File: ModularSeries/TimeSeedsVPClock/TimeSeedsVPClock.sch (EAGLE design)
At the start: 75 parts, among them T1 2N3904

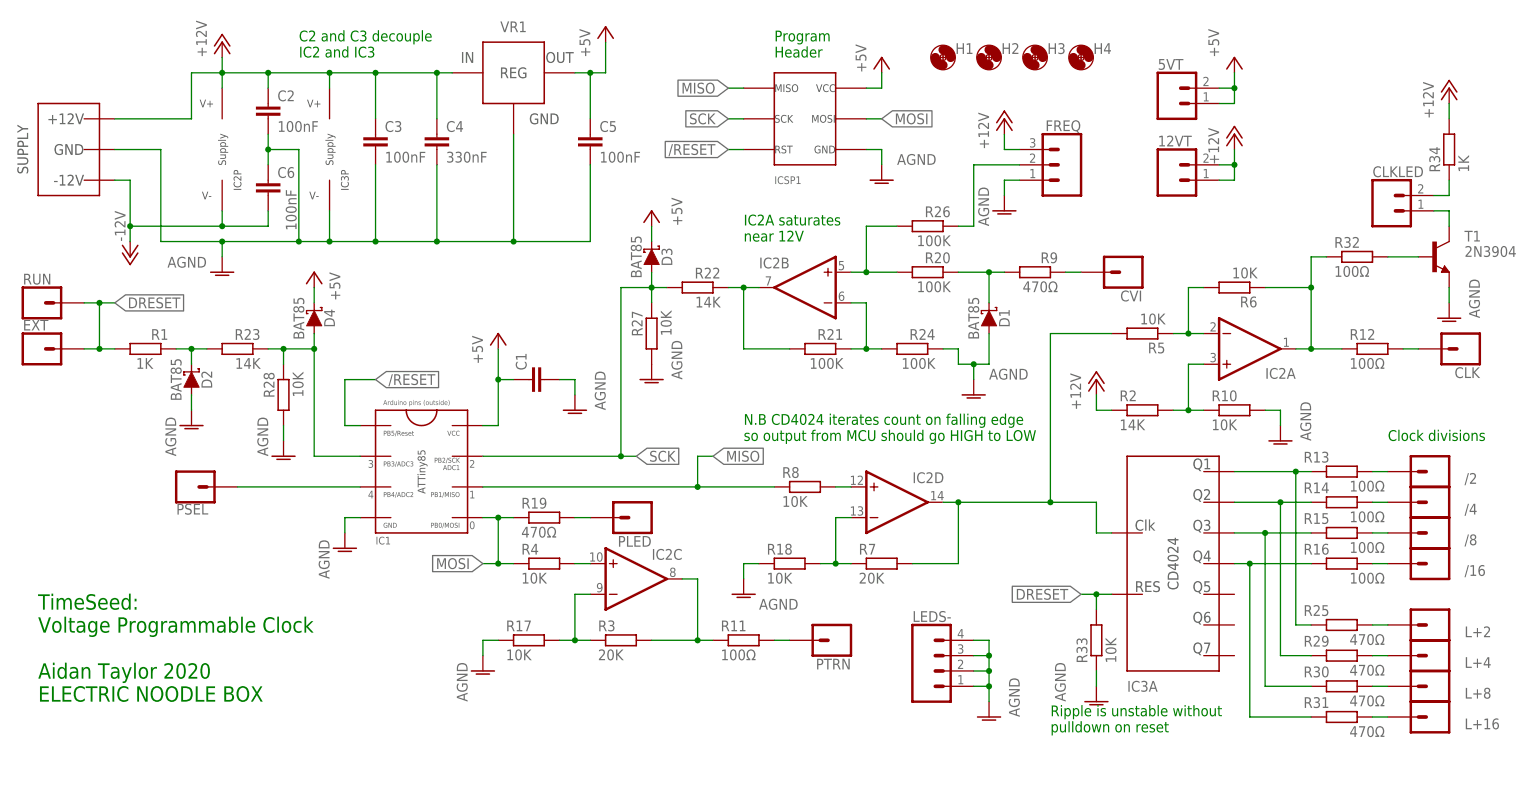
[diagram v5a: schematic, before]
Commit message: Pulse output fixed on Knives, schematics and layout updated. Panel added for Portals
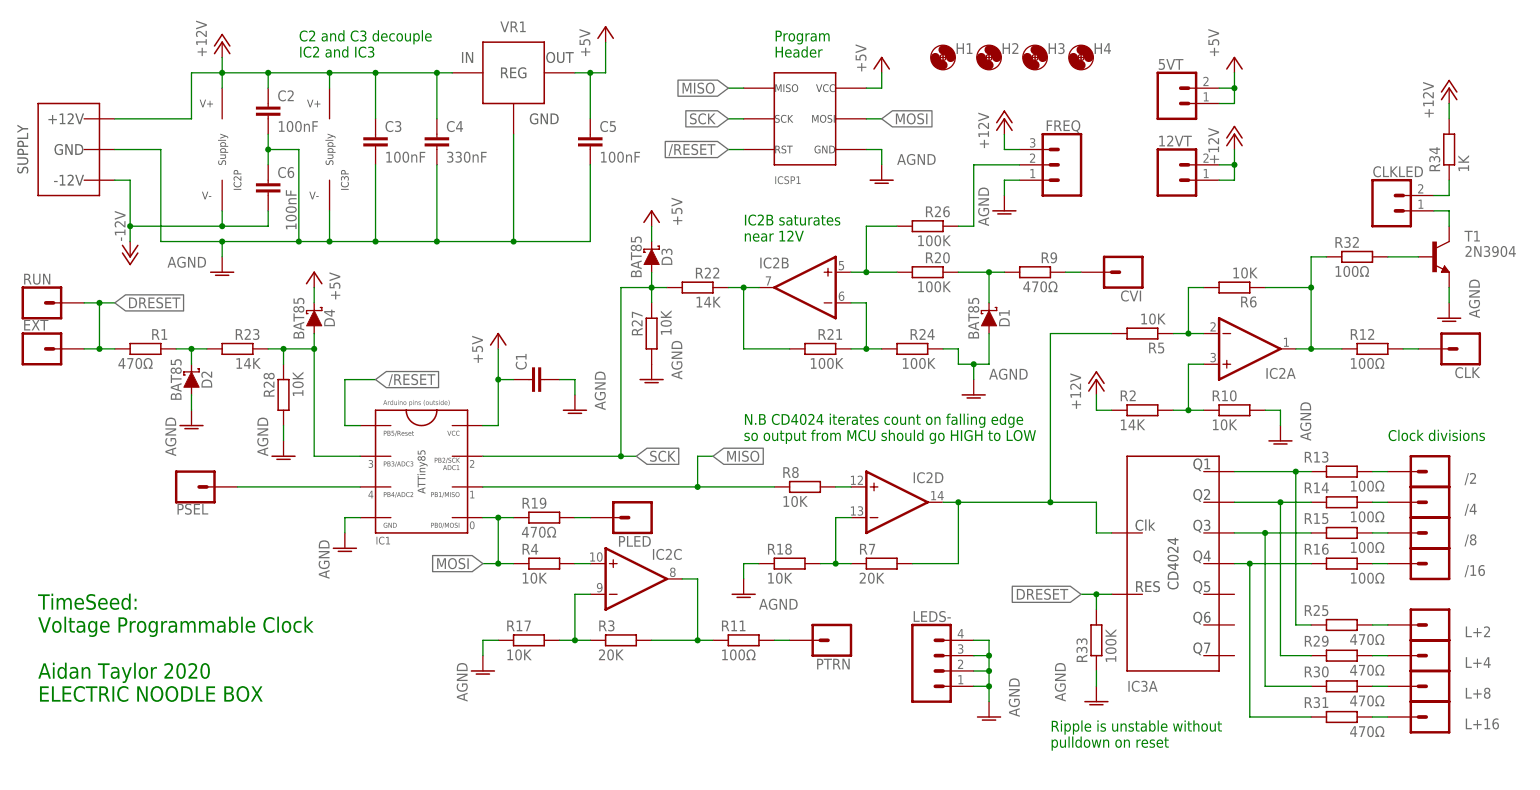
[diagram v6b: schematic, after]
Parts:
- R1: value 1K -> 470Ω
- R33: value 10K -> 100K
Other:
- note added: "IC2B saturates near 12V"
- note removed: "IC2A saturates near 12V"
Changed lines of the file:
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@@
 <part name="D3" library="ElectricNoodleBox" deviceset="SCHOTTKY_DO35" device="" package3d_urn="urn:adsk.eagle:package:43339/2" value="BAT85"/>
 <part name="P+8" library="supply1" library_urn="urn:adsk.eagle:library:371" deviceset="+5V" device=""/>
-<part name="R1" library="rcl" library_urn="urn:adsk.eagle:library:334" deviceset="R-EU_" device="0207/10" package3d_urn="urn:adsk.eagle:package:23491/2" value="1K"/>
+<part name="R1" library="rcl" library_urn="urn:adsk.eagle:library:334" deviceset="R-EU_" device="0207/10" package3d_urn="urn:adsk.eagle:package:23491/2" value="470Ω"/>
 <part name="AGND10" library="supply1" library_urn="urn:adsk.eagle:library:371" deviceset="AGND" device=""/>
 <part name="D4" library="ElectricNoodleBox" deviceset="SCHOTTKY_DO35" device="" package3d_urn="urn:adsk.eagle:package:43339/2" value="BAT85"/>
@@
 <part name="LEDS-" library="ElectricNoodleBox" deviceset="4XWIREPAD" device=""/>
 <part name="AGND7" library="supply1" library_urn="urn:adsk.eagle:library:371" deviceset="AGND" device=""/>
-<part name="R33" library="rcl" library_urn="urn:adsk.eagle:library:334" deviceset="R-EU_" device="0207/10" package3d_urn="urn:adsk.eagle:package:23491/2" value="10K"/>
+<part name="R33" library="rcl" library_urn="urn:adsk.eagle:library:334" deviceset="R-EU_" device="0207/10" package3d_urn="urn:adsk.eagle:package:23491/2" value="100K"/>
 <part name="AGND13" library="supply1" library_urn="urn:adsk.eagle:library:371" deviceset="AGND" device=""/>
 <part name="L+2" library="ElectricNoodleBox" deviceset="1XWIREPAD" device=""/>
@@
 Aidan Taylor 2020
 ELECTRIC NOODLE BOX</text>
-<text x="83.82" y="73.66" size="1.778" layer="91">IC2A saturates
+<text x="83.82" y="73.66" size="1.778" layer="91">IC2B saturates
 near 12V</text>
-<text x="134.62" y="-7.62" size="1.778" layer="91">Ripple is unstable without
+<text x="134.62" y="-10.16" size="1.778" layer="91">Ripple is unstable without
 pulldown on reset</text>
 <text x="83.82" y="40.64" size="1.778" layer="91">N.B CD4024 iterates count on falling edge

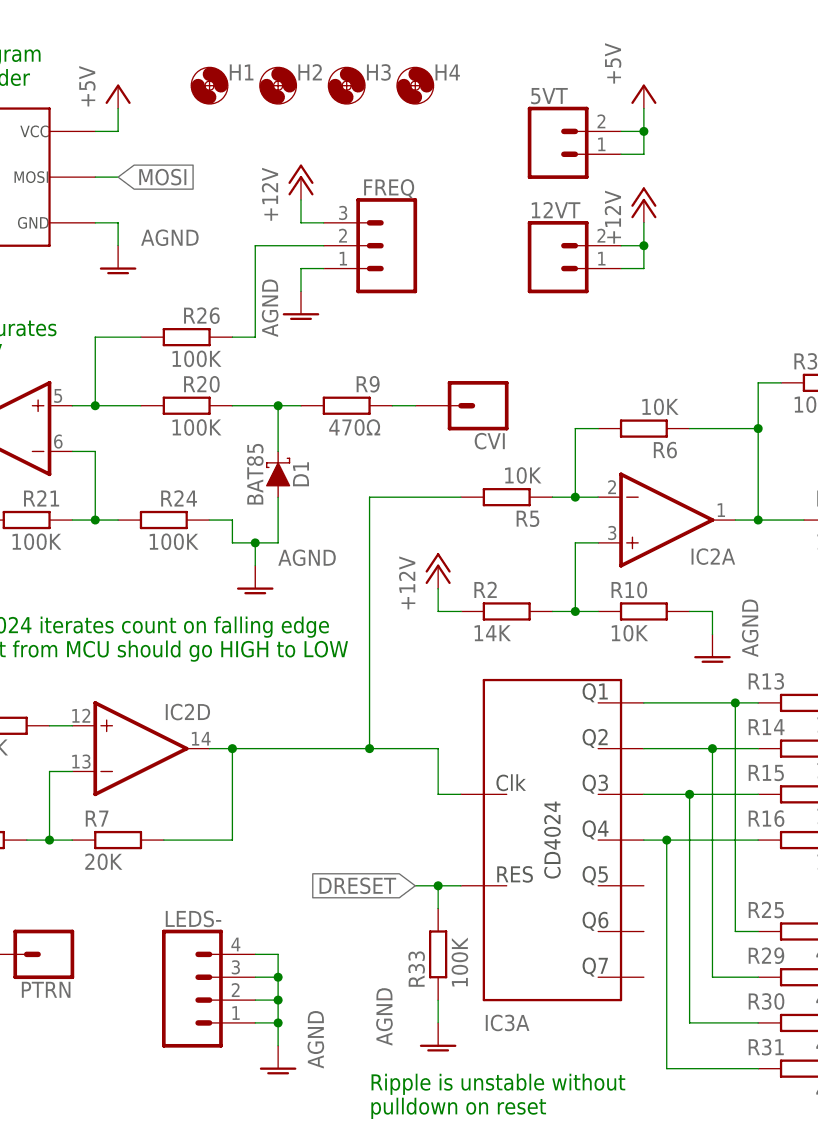
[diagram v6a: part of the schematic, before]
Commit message: Common collector + emitter follower pulse output added to Knives, docs updated
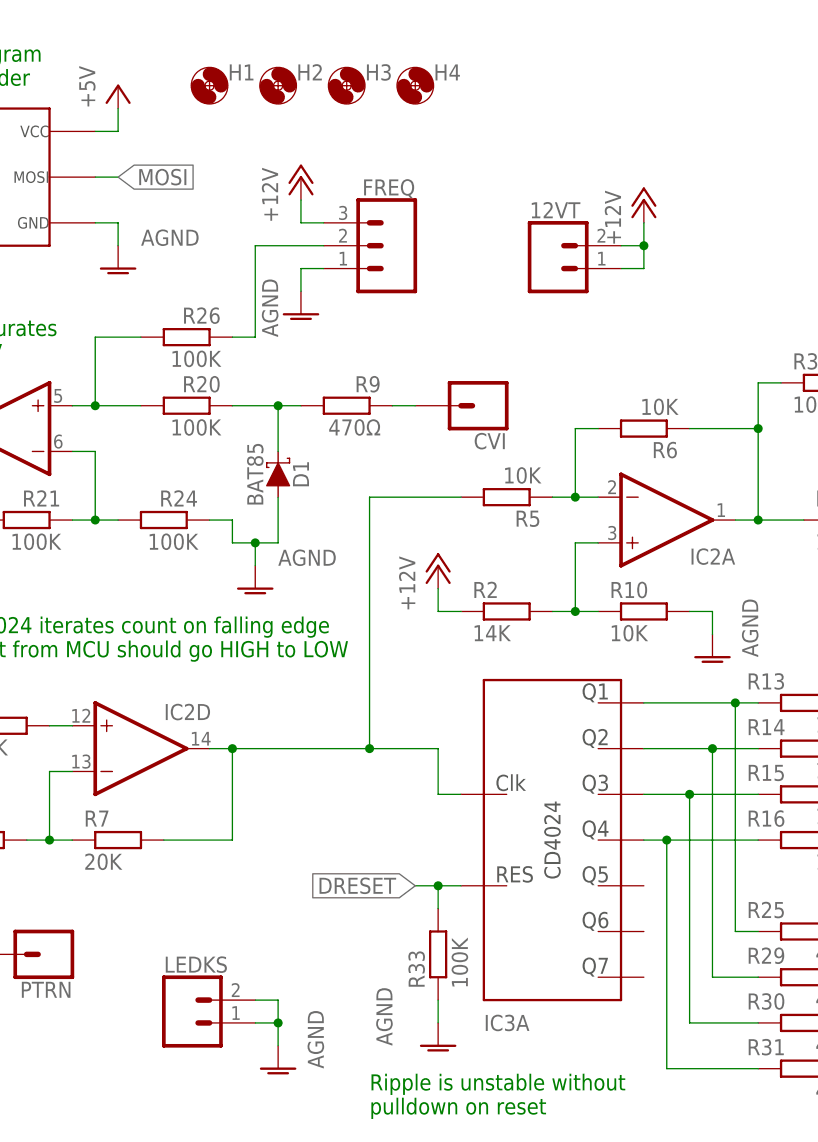
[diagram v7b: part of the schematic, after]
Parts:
- removed 5VT: 2XWIREPAD, ElectricNoodleBox:2XWIREPAD
- removed LEDS-: 4XWIREPAD, ElectricNoodleBox:4XWIREPAD
- added LEDKS: 2XWIREPAD, ElectricNoodleBox:2XWIREPAD
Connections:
- net +5V: no longer 5VT.1, 5VT.2
- net AGND: now also LEDKS.1, LEDKS.2; no longer LEDS-.1, LEDS-.2, LEDS-.3, LEDS-.4
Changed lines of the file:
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@@
 <part name="R31" library="rcl" library_urn="urn:adsk.eagle:library:334" deviceset="R-EU_" device="0207/10" package3d_urn="urn:adsk.eagle:package:23491/2" value="470Ω"/>
 <part name="C6" library="rcl" library_urn="urn:adsk.eagle:library:334" deviceset="C-EU" device="050-025X075" package3d_urn="urn:adsk.eagle:package:23637/1" value="100nF"/>
-<part name="LEDS-" library="ElectricNoodleBox" deviceset="4XWIREPAD" device=""/>
 <part name="AGND7" library="supply1" library_urn="urn:adsk.eagle:library:371" deviceset="AGND" device=""/>
 <part name="R33" library="rcl" library_urn="urn:adsk.eagle:library:334" deviceset="R-EU_" device="0207/10" package3d_urn="urn:adsk.eagle:package:23491/2" value="100K"/>
@@
 <part name="R34" library="rcl" library_urn="urn:adsk.eagle:library:334" deviceset="R-EU_" device="0207/10" package3d_urn="urn:adsk.eagle:package:23491/2" value="1K"/>
 <part name="AGND15" library="supply1" library_urn="urn:adsk.eagle:library:371" deviceset="AGND" device=""/>
-<part name="P+5" library="supply1" library_urn="urn:adsk.eagle:library:371" deviceset="+5V" device=""/>
 <part name="P+11" library="supply1" library_urn="urn:adsk.eagle:library:371" deviceset="+12V" device=""/>
-<part name="5VT" library="ElectricNoodleBox" deviceset="2XWIREPAD" device=""/>
 <part name="12VT" library="ElectricNoodleBox" deviceset="2XWIREPAD" device=""/>
 <part name="WP1" library="ElectricNoodleBox" deviceset="COMBO_SUPPLY_HEADER" device=""/>
+<part name="LEDKS" library="ElectricNoodleBox" deviceset="2XWIREPAD" device=""/>
 </parts>
 <sheets>
@@
 <attribute name="VALUE" x="8.001" y="82.296" size="1.778" layer="96" rot="R270"/>
 </instance>
-<instance part="LEDS-" gate="G$1" x="116.84" y="2.54" smashed="yes">
-<attribute name="NAME" x="111.76" y="10.668" size="1.778" layer="95" font="vector"/>
-</instance>
 <instance part="AGND7" gate="VR1" x="124.46" y="-5.08" smashed="yes">
 <attribute name="VALUE" x="129.54" y="-5.08" size="1.778" layer="96" rot="R90"/>
@@
 <attribute name="VALUE" x="-5.08" y="71.12" size="1.778" layer="96" rot="R180"/>
 </instance>
-<instance part="P+5" gate="1" x="165.1" y="104.14" smashed="yes">
-<attribute name="VALUE" x="162.56" y="104.14" size="1.778" layer="96" rot="R90"/>
-</instance>
 <instance part="P+11" gate="1" x="165.1" y="91.44" smashed="yes">
 <attribute name="VALUE" x="162.56" y="86.36" size="1.778" layer="96" rot="R90"/>
 </instance>
-<instance part="5VT" gate="G$1" x="154.94" y="96.52" smashed="yes">
-<attribute name="NAME" x="152.4" y="102.108" size="1.778" layer="95" font="vector"/>
-</instance>
 <instance part="12VT" gate="G$1" x="154.94" y="83.82" smashed="yes">
 <attribute name="NAME" x="152.4" y="89.408" size="1.778" layer="95" font="vector"/>
 </instance>
 <instance part="WP1" gate="G$1" x="-27.94" y="88.9" smashed="yes" rot="MR0"/>
+<instance part="LEDKS" gate="G$1" x="114.3" y="0" smashed="yes">
+<attribute name="NAME" x="111.76" y="5.588" size="1.778" layer="95" font="vector"/>
+</instance>
 </instances>
 <busses>
@@
 </segment>
 <segment>
-<pinref part="LEDS-" gate="G$1" pin="4"/>
-<wire x1="121.92" y1="7.62" x2="124.46" y2="7.62" width="0.1524" layer="91"/>
-<wire x1="124.46" y1="7.62" x2="124.46" y2="5.08" width="0.1524" layer="91"/>
-<pinref part="LEDS-" gate="G$1" pin="1"/>
-<wire x1="124.46" y1="5.08" x2="124.46" y2="2.54" width="0.1524" layer="91"/>
 <wire x1="124.46" y1="2.54" x2="124.46" y2="0" width="0.1524" layer="91"/>
 <wire x1="124.46" y1="0" x2="121.92" y2="0" width="0.1524" layer="91"/>
-<pinref part="LEDS-" gate="G$1" pin="2"/>
 <wire x1="121.92" y1="2.54" x2="124.46" y2="2.54" width="0.1524" layer="91"/>
-<junction x="124.46" y="2.54"/>
-<pinref part="LEDS-" gate="G$1" pin="3"/>
-<wire x1="121.92" y1="5.08" x2="124.46" y2="5.08" width="0.1524" layer="91"/>
-<junction x="124.46" y="5.08"/>
 <pinref part="AGND7" gate="VR1" pin="AGND"/>
 <wire x1="124.46" y1="0" x2="124.46" y2="-2.54" width="0.1524" layer="91"/>
 <junction x="124.46" y="0"/>
+<pinref part="LEDKS" gate="G$1" pin="1"/>
+<pinref part="LEDKS" gate="G$1" pin="2"/>
 </segment>
 <segment>
@@
 <wire x1="12.7" y1="66.04" x2="12.7" y2="63.5" width="0.1524" layer="91"/>
 </segment>
-<segment>
-<pinref part="5VT" gate="G$1" pin="1"/>
-<wire x1="162.56" y1="96.52" x2="165.1" y2="96.52" width="0.1524" layer="91"/>
-<pinref part="5VT" gate="G$1" pin="2"/>
-<wire x1="165.1" y1="96.52" x2="165.1" y2="99.06" width="0.1524" layer="91"/>
-<wire x1="162.56" y1="99.06" x2="165.1" y2="99.06" width="0.1524" layer="91"/>
-<pinref part="P+5" gate="1" pin="+5V"/>
-<wire x1="165.1" y1="99.06" x2="165.1" y2="101.6" width="0.1524" layer="91"/>
-<junction x="165.1" y="99.06"/>
-</segment>
 </net>

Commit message: TimeSeed files updated for production
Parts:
- C1: value (none) -> 100nF
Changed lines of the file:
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@@
 <?xml version="1.0" encoding="utf-8"?>
 <!DOCTYPE eagle SYSTEM "eagle.dtd">
-<eagle version="9.6.0">
+<eagle version="9.6.2">
 <drawing>
 <settings>
@@
 <part name="P-1" library="supply1" library_urn="urn:adsk.eagle:library:371" deviceset="-12V" device=""/>
 <part name="ICSP1" library="ElectricNoodleBox" deviceset="ICSP_2.54" device=""/>
-<part name="C1" library="rcl" library_urn="urn:adsk.eagle:library:334" deviceset="C-EU" device="050-025X075" package3d_urn="urn:adsk.eagle:package:23637/1"/>
+<part name="C1" library="rcl" library_urn="urn:adsk.eagle:library:334" deviceset="C-EU" device="050-025X075" package3d_urn="urn:adsk.eagle:package:23637/1" value="100nF"/>
 <part name="AGND2" library="supply1" library_urn="urn:adsk.eagle:library:371" deviceset="AGND" device=""/>
 <part name="P+2" library="supply1" library_urn="urn:adsk.eagle:library:371" deviceset="+5V" device=""/>
